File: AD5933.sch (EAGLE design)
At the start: 48 parts, among them U1 ADG1604BRUZ, U10 ADP3303ARZ-3.3, U12 AD5245BRJZ100-R2, U2 AD5933YRSZ, U3 ADG1604BRUZ, U4 AD8606ARZ, U5 ADG1604BRUZ, U6 ADG1604BRUZ, U7 AD8606ARZ, U8 LTC6904MPMS8TRPBF, X1 DC21MMX

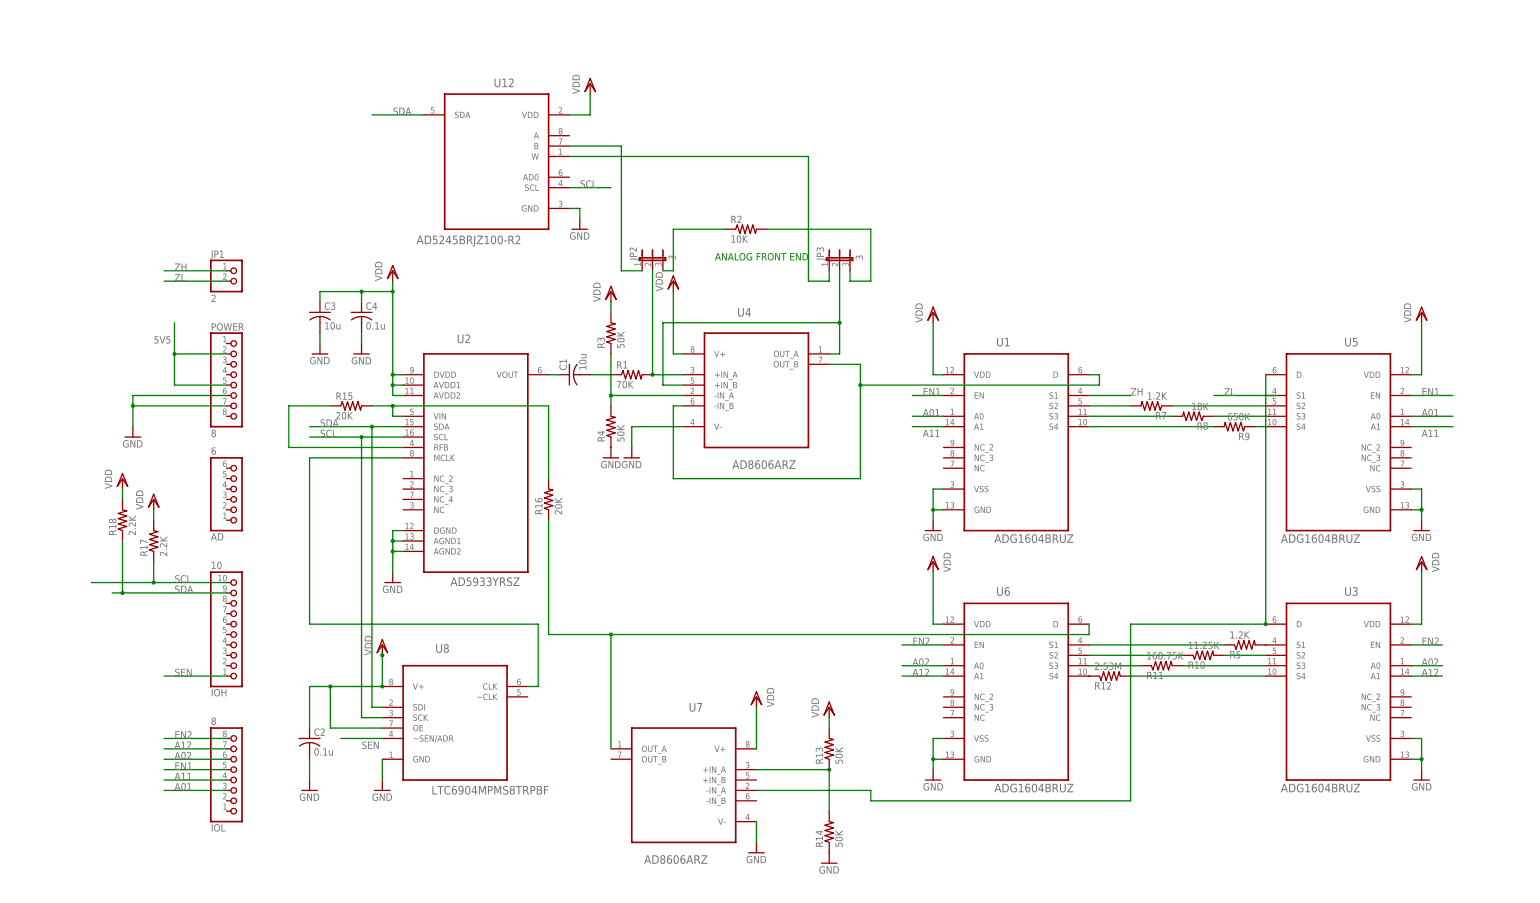
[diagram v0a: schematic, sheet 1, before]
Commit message: Seperate VDD,VCC(Analog) added bypass capacitors to all chips
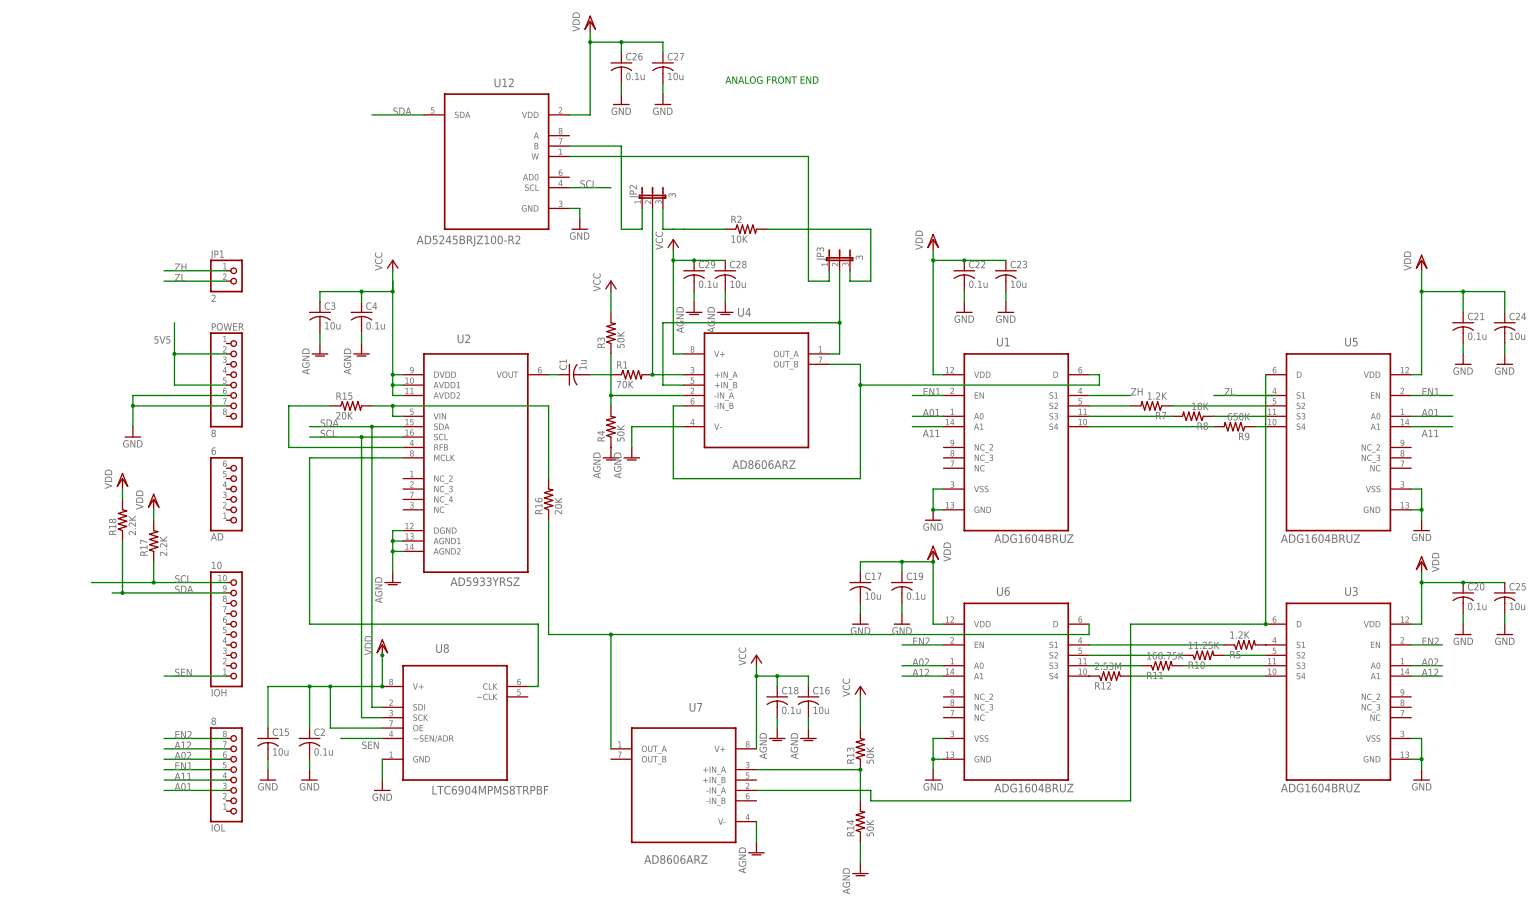
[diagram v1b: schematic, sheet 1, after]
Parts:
- removed PWR_LED: GREEN, led:LEDCHIP-LED0805
- added ANALOG_PWR, DIGITAL_PWR: GREEN, led:LEDCHIP-LED0805
- added C13, C15, C16, C17, C23, C24, C25, C27, C28, C5: 10u, rcl:C-USC0805
- added C14, C18, C19, C20, C21, C22, C26, C29, C6, C7: 0.1u, rcl:C-USC0805
- added R19: 1K, rcl:R-US_M0805
- added U9: ADP3303ARZ-3.3, Analog Devices_By_element14_Batch_1:ADP3303ARZ-3.3
- C1: value 10u -> 1u
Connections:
- removed net N$31: C10.1, C8.1, JP4.2, U10.IN, U10.IN_2, U10.~SD
- new net AGND: ANALOG_PWR.C, C10.2, C11.2, C13.2, C16.2, C18.2, C2.2, C28.2, C29.2, C3.2, C4.2, C5.2, C6.2, C7.2, C8.2, C9.2, DIGITAL_PWR.C, POWER.6, POWER.7, R14.1, R4.1, U1.GND, U1.VSS, U10.GND, U12.GND, U2.AGND1, U2.AGND2, U2.DGND, U3.GND, U3.VSS, U4.V-, U5.GND, U5.VSS, U6.GND, U6.VSS, U7.V-, U8.GND, U9.GND, X1.1, X1.3
- new net N$34: ANALOG_PWR.A, R19.1
- new net N$36: C10.1, C13.1, C7.1, C8.1, JP4.2, U10.IN, U10.IN_2, U10.~SD, U9.IN, U9.IN_2, U9.~SD
- new net N$38: C14.1, U9.NR
- new net VCC: C14.2, C16.1, C18.1, C28.1, C29.1, C3.1, C4.1, C5.1, C6.1, R13.2, R19.2, R3.2, U2.AVDD1, U2.AVDD2, U2.DVDD, U4.V+, U7.V+, U9.OUT, U9.OUT_2
- net GND: now also C15.2, C17.2, C19.2, C20.2, C21.2, C22.2, C23.2, C24.2, C25.2, C26.2, C27.2; no longer C10.2, C11.2, C2.2, C3.2, C4.2, C8.2, C9.2, POWER.6, POWER.7, PWR_LED.C, R14.1, R4.1, U1.GND, U1.VSS, U10.GND, U12.GND, U2.AGND1, U2.AGND2, U2.DGND, U3.GND, U3.VSS, U4.V-, U5.GND, U5.VSS, U6.GND, U6.VSS, U7.V-, U8.GND, X1.1, X1.3
- net N$20: now also DIGITAL_PWR.A; no longer PWR_LED.A
- net VDD: now also C15.1, C17.1, C19.1, C20.1, C21.1, C22.1, C23.1, C24.1, C25.1, C26.1, C27.1; no longer C3.1, C4.1, R13.2, R3.2, U2.AVDD1, U2.AVDD2, U2.DVDD, U4.V+, U7.V+
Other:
- note added: "5V5 to 3V3 regulator : Analog Supply"
- note added: "5V5 to 3V3 regulator : Digital Supply"
- note removed: "5V5 to 3V3 regulator"
- moved on the sheet: C10, JP2, JP4, R13, R14

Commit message: Add digipots
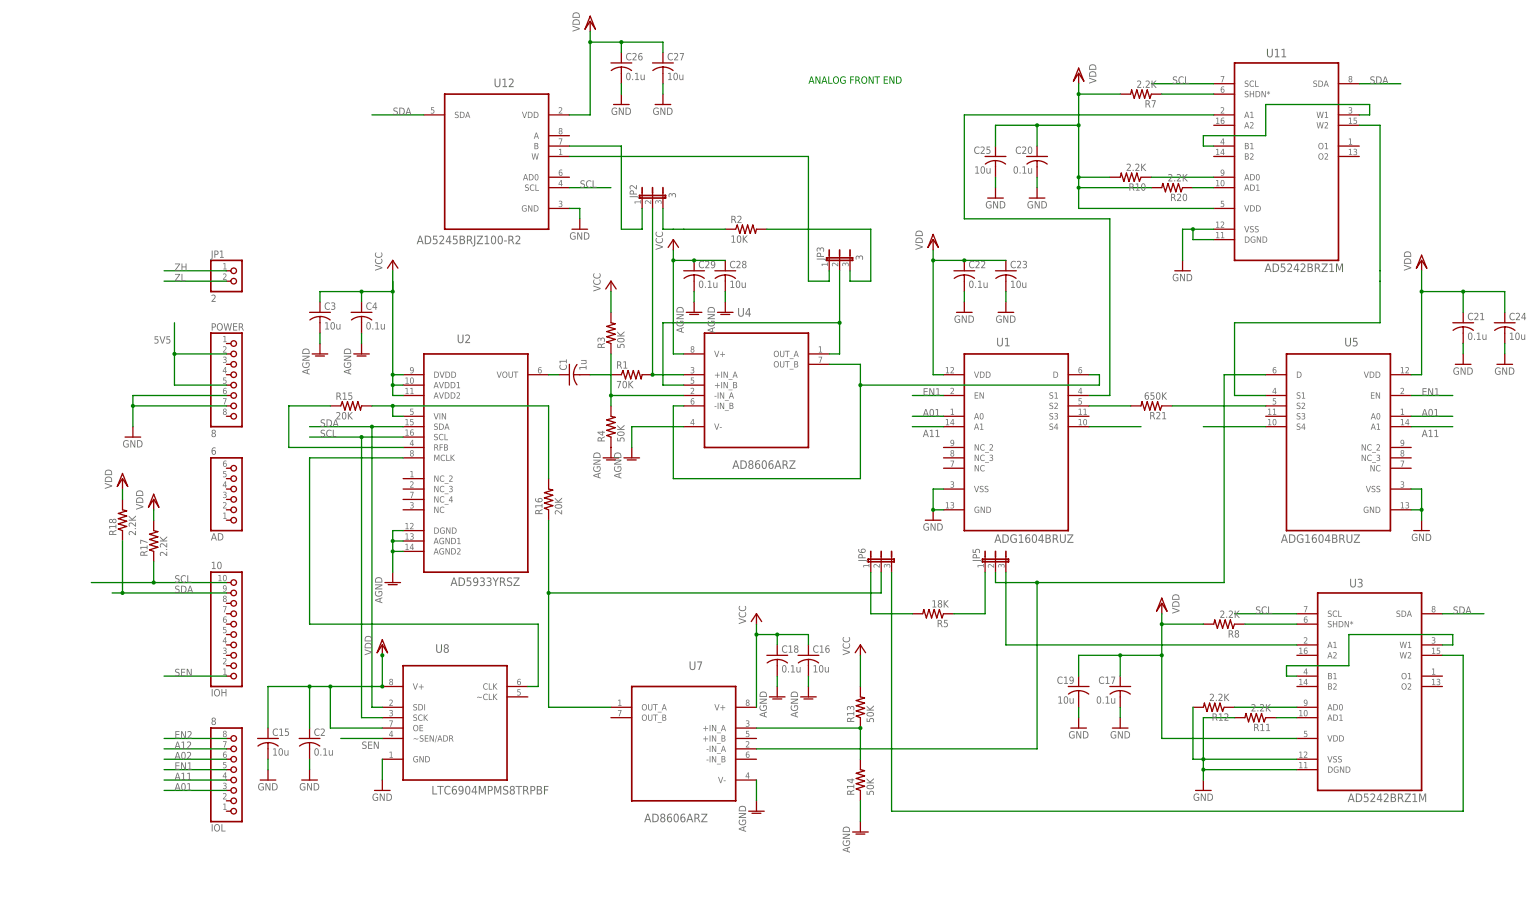
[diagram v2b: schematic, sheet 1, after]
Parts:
- removed R9: 650K, rcl:R-US_M0805
- removed U6: ADG1604BRUZ, Analog Devices_By_element14_Batch_1:ADG1604BRUZ
- added JP5, JP6: (no value), jumper:JP2E
- added R20: 2.2K, rcl:R-US_M0805
- added R21: 650K, rcl:R-US_M0805
- added U11: AD5242BRZ1M, ADI Batch_2:AD5242BRZ1M
- C17: value 10u -> 0.1u
- C19: value 0.1u -> 10u
- R10: value 11.25K -> 2.2K
- R11: value 168.75K -> 2.2K
- R12: value 2.53M -> 2.2K
- R5: value 1.2K -> 18K
- R7: value 1.2K -> 2.2K
- R8: value 18K -> 2.2K
- U3: value ADG1604BRUZ -> AD5242BRZ1M; device Analog Devices_By_element14_Batch_1:ADG1604BRUZ -> ADI Batch_2:AD5242BRZ1M
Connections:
- new net N$31: R20.1, U11.AD1
- new net N$39: U11.B1, U11.W1
- new net N$40: U5.S4
- new net N$7: JP5.1, R5.1
- net A02: no longer U3.A0, U6.A0
- net A12: no longer U3.A1, U6.A1
- net AGND: no longer U3.GND, U3.VSS, U6.GND, U6.VSS
- net EN2: no longer U3.EN, U6.EN
- net GND: now also R11.2, R12.2, U11.DGND, U11.VSS, U3.DGND, U3.VSS
- net N$10: now also R7.1, U11.SHDN*; no longer R9.2, U1.S4
- net N$12: now also JP5.2, U5.D, U7.-IN_A; no longer R7.1, U5.S2
- net N$13: now also R21.1, U5.S2; no longer R8.1, U5.S3
- net N$14: now also U1.S4; no longer R9.1, U5.S4
- net N$23: now also JP5.3, U3.A1; no longer R5.2, U3.S1
- net N$24: now also U11.W2, U5.S1; no longer R10.2, U3.S2
- net N$25: now also U3.B1, U3.W1; no longer R11.2, U3.S3
- net N$26: now also R12.1, U3.AD0; no longer R12.2, U3.S4
- net N$27: now also JP6.3, U3.W2; no longer R5.1, U6.S1
- net N$28: now also JP6.1, R5.2; no longer R10.1, U6.S2
- net N$29: now also U3.AD1; no longer U6.S3
- net N$30: now also R10.1, U11.AD0; no longer R12.1, U6.S4
- net N$32: now also R8.1, U3.SHDN*; no longer U3.D, U5.D, U7.-IN_A
- net N$5: now also JP6.2; no longer U6.D
- net N$8: now also R21.2; no longer R7.2
- net N$9: now also U1.S1, U11.A1; no longer R8.2, U1.S3
- net SCL: now also U11.SCL, U3.SCL
- net SDA: now also U11.SDA, U3.SDA
- net VDD: now also R10.2, R20.2, R7.2, R8.2, U11.VDD; no longer U6.VDD
- net ZH: no longer U1.S1
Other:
- moved on the sheet: C16, C17, C18, C19, C20, C25, R10, R11, R12, R13, R14, R5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

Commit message: Review DRC error
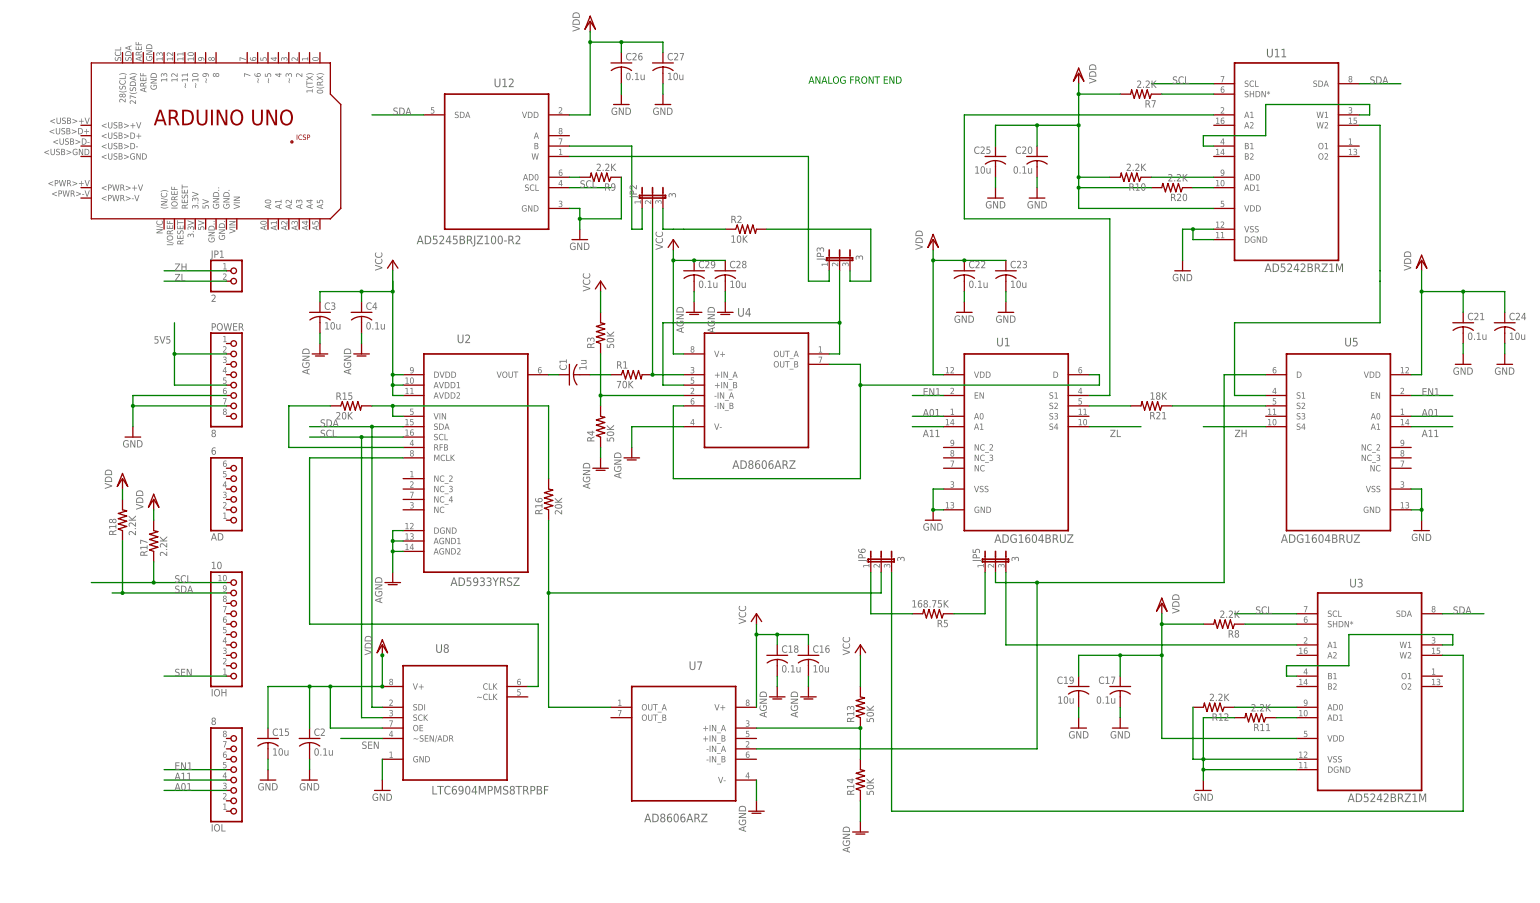
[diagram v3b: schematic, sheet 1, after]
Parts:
- added PCB1: ARDUINO_UNO, E14_Arduino_revC:ARDUINO_UNO
- added R9: 2.2K, rcl:R-US_M0805
- JP5, JP6: value (none) -> 3
- R21: value 650K -> 18K
- R5: value 18K -> 168.75K
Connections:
- removed net A02: IOL.6
- removed net A12: IOL.7
- removed net EN2: IOL.8
- removed net N$40: U5.S4
- net AGND: no longer C10.2, C11.2, C2.2, C8.2, C9.2, DIGITAL_PWR.C, POWER.6, POWER.7, U1.GND, U1.VSS, U10.GND, U12.GND, U5.GND, U5.VSS, U8.GND, X1.1, X1.3
- net GND: now also C10.2, C11.2, C2.2, C8.2, C9.2, DIGITAL_PWR.C, POWER.6, POWER.7, R9.1, U1.GND, U1.VSS, U10.GND, U12.GND, U5.GND, U5.VSS, U8.GND, X1.1, X1.3
- net N$14: now also R9.2, U12.AD0; no longer U1.S4
- net ZH: now also U5.S4
- net ZL: now also U1.S4
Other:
- moved on the sheet: C10, C8, R3, R4

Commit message: Move analog muxes to analog power domain
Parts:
- C15: value 10u -> 1u
- PCB1: value ARDUINO_UNO -> ARDUINO_MEGA2560; device E14_Arduino_revC:ARDUINO_UNO -> E14_Arduino_revC:ARDUINO_MEGA2560
- R19, R6: value 1K -> 325
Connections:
- net AGND: now also U1.GND, U1.VSS, U5.GND, U5.VSS
- net GND: no longer U1.GND, U1.VSS, U5.GND, U5.VSS
- net VCC: now also C21.1, C22.1, C23.1, C24.1, U1.VDD, U5.VDD
- net VDD: no longer C21.1, C22.1, C23.1, C24.1, U1.VDD, U5.VDD
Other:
- note added: "1A, 1000V"
- note added: "Add via to short Vcc and Vdd if you do not get 2 AD3303 IC"
- note added: "If = 2mA, Vf = 2.65V"

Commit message: Replace IC from old libray name to new library name(same library)
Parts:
- U1, U5: device Analog Devices_By_element14_Batch_1:ADG1604BRUZ -> ADI Batch_1:ADG1604BRUZ
- U10, U9: device Analog Devices_By_element14_Batch_1:ADP3303ARZ-3.3 -> ADI Batch_1:ADP3303ARZ-3.3
- U2: device Analog Devices_By_element14_Batch_1:AD5933YRSZ -> ADI Batch_1:AD5933YRSZ
- U4, U7: device Analog Devices_By_element14_Batch_1:AD8606ARZ -> ADI Batch_1:AD8606ARZ
- U8: device LTC_By_element14_Batch_1:LTC6904MPMS8TRPBF -> LTC_Batch_1:LTC6904MPMS8TRPBF
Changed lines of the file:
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@@
 </classes>
 <parts>
-<part name="U2" library="Analog Devices_By_element14_Batch_1" deviceset="AD5933YRSZ" device=""/>
-<part name="U1" library="Analog Devices_By_element14_Batch_1" deviceset="ADG1604BRUZ" device=""/>
-<part name="U4" library="Analog Devices_By_element14_Batch_1" deviceset="AD8606ARZ" device=""/>
+<part name="U2" library="ADI Batch_1" deviceset="AD5933YRSZ" device=""/>
+<part name="U1" library="ADI Batch_1" deviceset="ADG1604BRUZ" device=""/>
+<part name="U4" library="ADI Batch_1" deviceset="AD8606ARZ" device=""/>
 <part name="R1" library="rcl" deviceset="R-US_" device="M0805" value="70K"/>
 <part name="R2" library="rcl" deviceset="R-US_" device="M0805" value="10K"/>
@@
 <part name="GND1" library="supply1" deviceset="AGND" device=""/>
 <part name="GND3" library="supply1" deviceset="AGND" device=""/>
-<part name="U5" library="Analog Devices_By_element14_Batch_1" deviceset="ADG1604BRUZ" device=""/>
-<part name="U7" library="Analog Devices_By_element14_Batch_1" deviceset="AD8606ARZ" device=""/>
+<part name="U5" library="ADI Batch_1" deviceset="ADG1604BRUZ" device=""/>
+<part name="U7" library="ADI Batch_1" deviceset="AD8606ARZ" device=""/>
 <part name="R13" library="rcl" deviceset="R-US_" device="M0805" value="50K"/>
 <part name="R14" library="rcl" deviceset="R-US_" device="M0805" value="50K"/>
@@
 <part name="R15" library="rcl" deviceset="R-US_" device="M0805" value="20K"/>
 <part name="R16" library="rcl" deviceset="R-US_" device="M0805" value="20K"/>
-<part name="U8" library="LTC_By_element14_Batch_1" deviceset="LTC6904MPMS8TRPBF" device=""/>
+<part name="U8" library="LTC_Batch_1" deviceset="LTC6904MPMS8TRPBF" device=""/>
 <part name="VDD10" library="supply1" deviceset="VDD" device=""/>
 <part name="GND10" library="supply1" deviceset="GND" device=""/>
@@
 <part name="IOL" library="pinhead" deviceset="PINHD-1X8" device="" value="8"/>
 <part name="GND18" library="supply1" deviceset="GND" device=""/>
-<part name="U10" library="Analog Devices_By_element14_Batch_1" deviceset="ADP3303ARZ-3.3" device=""/>
+<part name="U10" library="ADI Batch_1" deviceset="ADP3303ARZ-3.3" device=""/>
 <part name="GND19" library="supply1" deviceset="GND" device=""/>
 <part name="C8" library="rcl" deviceset="C-US" device="C0805" value="0.1u"/>
@@
 <part name="GND14" library="supply1" deviceset="AGND" device=""/>
 <part name="GND15" library="supply1" deviceset="AGND" device=""/>
-<part name="U9" library="Analog Devices_By_element14_Batch_1" deviceset="ADP3303ARZ-3.3" device=""/>
+<part name="U9" library="ADI Batch_1" deviceset="ADP3303ARZ-3.3" device=""/>
 <part name="C5" library="rcl" deviceset="C-US" device="C0805" value="10u"/>
 <part name="C6" library="rcl" deviceset="C-US" device="C0805" value="0.1u"/>
